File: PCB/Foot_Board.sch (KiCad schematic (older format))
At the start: 7 parts, among them J7 Conn_02x03_Counter_Clockwise

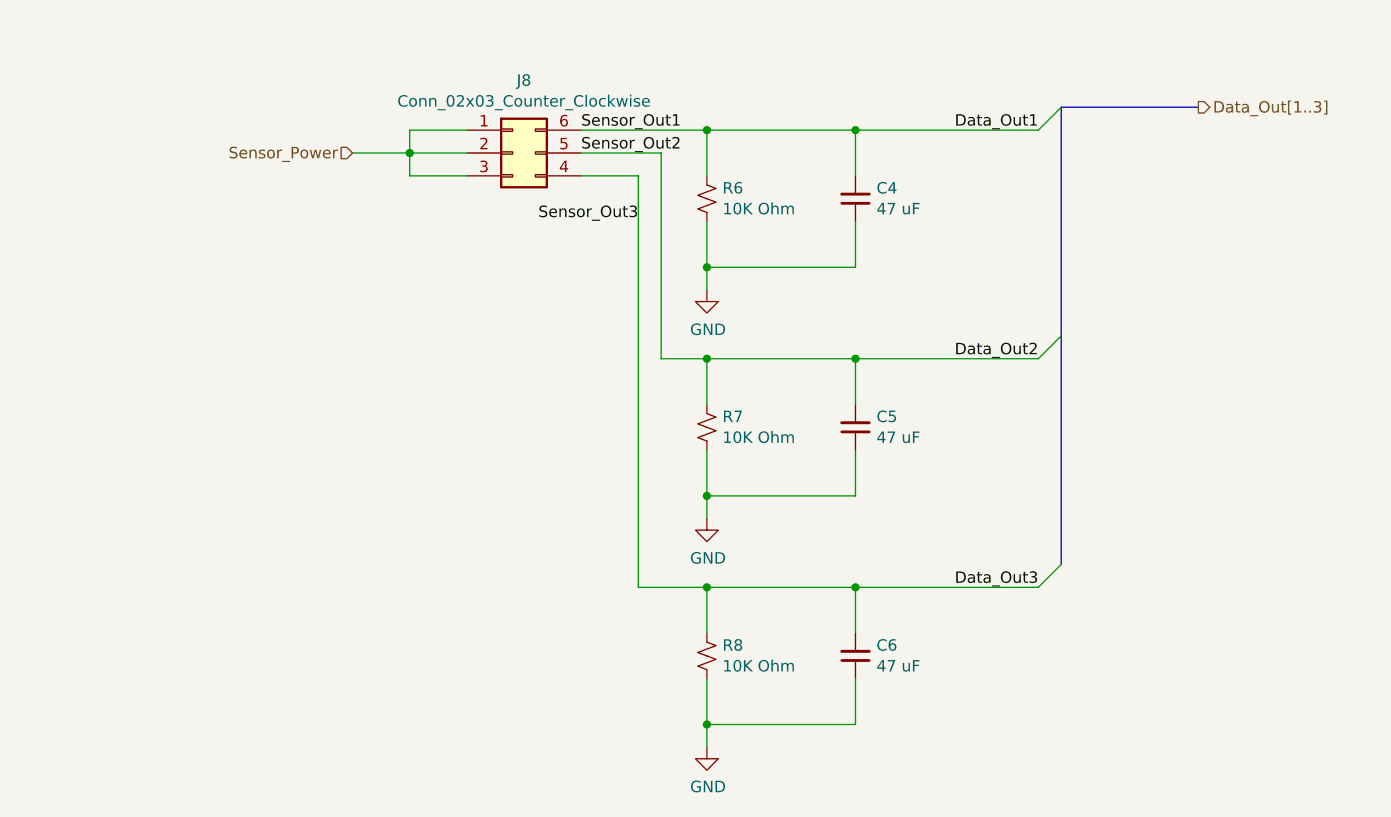
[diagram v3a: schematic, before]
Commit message: Added power LED
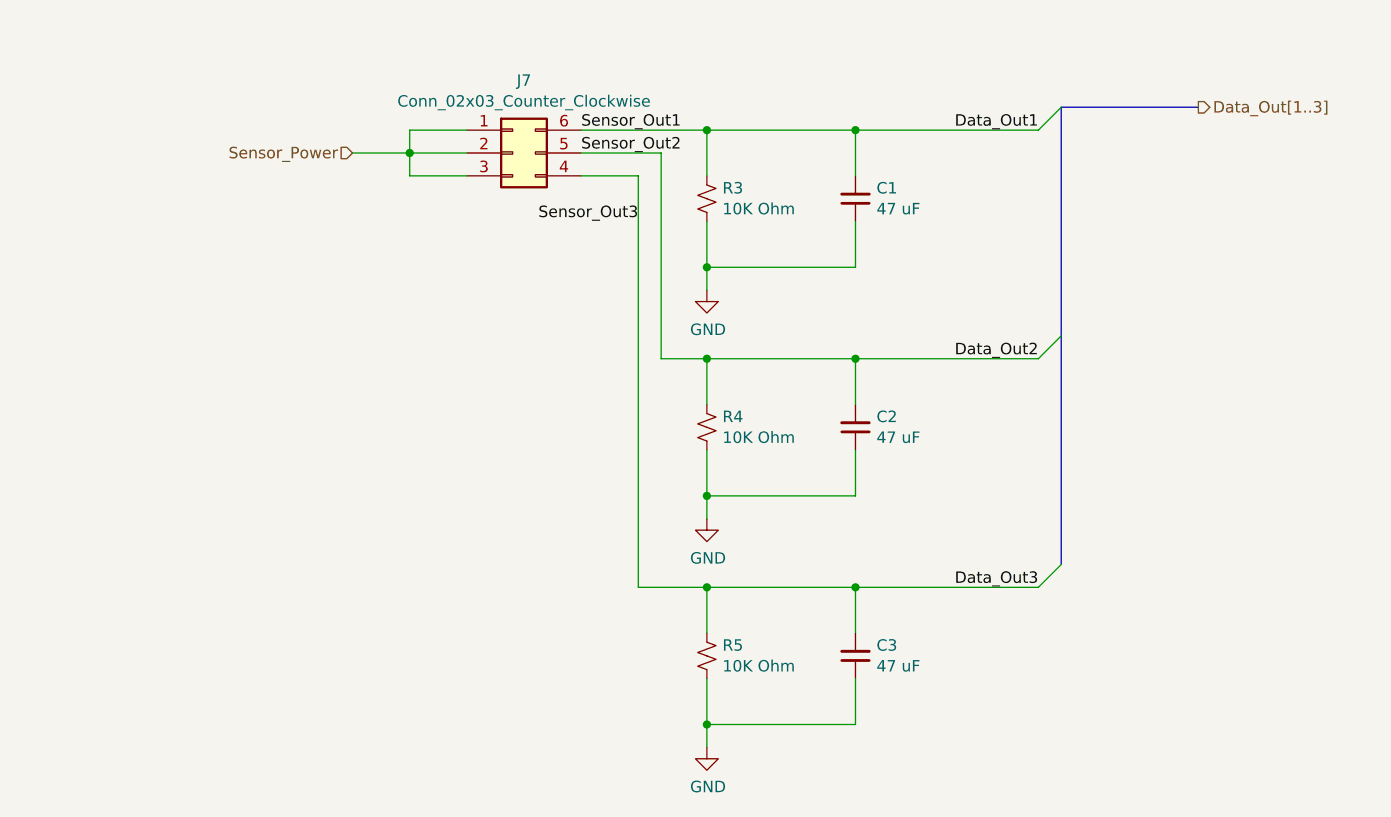
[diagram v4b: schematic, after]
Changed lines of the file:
@@
 AR Path="/611C8367/611C4CD5" Ref="C1"  Part="1"
 AR Path="/611CB06B/611C4CD5" Ref="C4"  Part="1"
-F 0 "C4" H 6308 2654 50  0000 R CNN
+F 0 "C1" H 6308 2654 50  0000 R CNN
 F 1 "47 uF" H 6308 2745 50  0000 R CNN
 F 2 "Capacitor_THT:CP_Radial_D5.0mm_P2.50mm" H 6400 2700 50  0001 C CNN
@@
 AR Path="/611C8367/611C4CDB" Ref="R3"  Part="1"
 AR Path="/611CB06B/611C4CDB" Ref="R6"  Part="1"
-F 0 "R6" H 5818 2746 50  0000 L CNN
+F 0 "R3" H 5818 2746 50  0000 L CNN
 F 1 "10K Ohm" H 5818 2655 50  0000 L CNN
 F 2 "Resistor_THT:R_Axial_DIN0207_L6.3mm_D2.5mm_P7.62mm_Horizontal" H 5750 2700 50  0001 C CNN
@@
 AR Path="/611C8367/611C4CE1" Ref="#PWR010"  Part="1"
 AR Path="/611CB06B/611C4CE1" Ref="#PWR013"  Part="1"
-F 0 "#PWR013" H 5750 2850 50  0001 C CNN
+F 0 "#PWR010" H 5750 2850 50  0001 C CNN
 F 1 "GND" H 5755 2927 50  0000 C CNN
 F 2 "" H 5750 3100 50  0000 C CNN
@@
 AR Path="/611C8367/611CFFCC" Ref="#PWR011"  Part="1"
 AR Path="/611CB06B/611CFFCC" Ref="#PWR014"  Part="1"
-F 0 "#PWR014" H 5750 3850 50  0001 C CNN
+F 0 "#PWR011" H 5750 3850 50  0001 C CNN
 F 1 "GND" H 5755 3927 50  0000 C CNN
 F 2 "" H 5750 4100 50  0000 C CNN
@@
 AR Path="/611C8367/611D0D36" Ref="#PWR012"  Part="1"
 AR Path="/611CB06B/611D0D36" Ref="#PWR015"  Part="1"
-F 0 "#PWR015" H 5750 4850 50  0001 C CNN
+F 0 "#PWR012" H 5750 4850 50  0001 C CNN
 F 1 "GND" H 5755 4927 50  0000 C CNN
 F 2 "" H 5750 5100 50  0000 C CNN
@@
 AR Path="/611C8367/611D5C2C" Ref="J7"  Part="1"
 AR Path="/611CB06B/611D5C2C" Ref="J8"  Part="1"
-F 0 "J8" H 4950 2817 50  0000 C CNN
+F 0 "J7" H 4950 2817 50  0000 C CNN
 F 1 "Conn_02x03_Counter_Clockwise" H 4950 2726 50  0000 C CNN
 F 2 "Connector_Molex:Molex_Micro-Fit_3.0_43045-0600_2x03_P3.00mm_Horizontal" H 4900 2500 50  0001 C CNN
@@
 AR Path="/611C8367/611E994E" Ref="C2"  Part="1"
 AR Path="/611CB06B/611E994E" Ref="C5"  Part="1"
-F 0 "C5" H 6308 3654 50  0000 R CNN
+F 0 "C2" H 6308 3654 50  0000 R CNN
 F 1 "47 uF" H 6308 3745 50  0000 R CNN
 F 2 "Capacitor_THT:CP_Radial_D5.0mm_P2.50mm" H 6400 3700 50  0001 C CNN
@@
 AR Path="/611C8367/611E9C41" Ref="C3"  Part="1"
 AR Path="/611CB06B/611E9C41" Ref="C6"  Part="1"
-F 0 "C6" H 6308 4654 50  0000 R CNN
+F 0 "C3" H 6308 4654 50  0000 R CNN
 F 1 "47 uF" H 6308 4745 50  0000 R CNN
 F 2 "Capacitor_THT:CP_Radial_D5.0mm_P2.50mm" H 6400 4700 50  0001 C CNN
@@
 Wire Wire Line
 	4450 2600 4450 2500
-Wire Bus Line
-	7300 2300 7300 4300
 $Comp
 L Device:R_Small_US R?
@@
 AR Path="/611C8367/611EC5B5" Ref="R4"  Part="1"
 AR Path="/611CB06B/611EC5B5" Ref="R7"  Part="1"
-F 0 "R7" H 5818 3746 50  0000 L CNN
+F 0 "R4" H 5818 3746 50  0000 L CNN
 F 1 "10K Ohm" H 5818 3655 50  0000 L CNN
 F 2 "Resistor_THT:R_Axial_DIN0207_L6.3mm_D2.5mm_P7.62mm_Horizontal" H 5750 3700 50  0001 C CNN
@@
 AR Path="/611C8367/611ECAE2" Ref="R5"  Part="1"
 AR Path="/611CB06B/611ECAE2" Ref="R8"  Part="1"
-F 0 "R8" H 5818 4746 50  0000 L CNN
+F 0 "R5" H 5818 4746 50  0000 L CNN
 F 1 "10K Ohm" H 5818 4655 50  0000 L CNN
 F 2 "Resistor_THT:R_Axial_DIN0207_L6.3mm_D2.5mm_P7.62mm_Horizontal" H 5750 4700 50  0001 C CNN
@@
 	1    0    0    -1
 $EndComp
+Wire Bus Line
+	7300 2300 7300 4300
 $EndSCHEMATC
